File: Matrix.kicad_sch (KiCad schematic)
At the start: 72 parts, among them SW1 SW_Push, SW10 SW_Push, SW11 SW_Push, SW12 SW_Push, SW13 SW_Push, SW14 SW_Push, SW15 SW_Push, SW16 SW_Push, SW17 SW_Push, SW18 SW_Push, SW2 SW_Push, SW3 SW_Push, SW4 SW_Push, SW5 SW_Push, SW6 SW_Push, SW7 SW_Push, SW8 SW_Push, SW9 SW_Push

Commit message: update power mgmt
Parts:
- removed D10, D14, D15, D16, D17, D2, D22, D23, D24, D25, D3, D30, D31, D32, D33, D4, D8, D9: LED, LED_SMD:LED_0603_1608Metric_Pad1.05x0.95mm_HandSolder, symbol Device:LED
- removed R10, R11, R12, R13, R14, R15, R16, R17, R18, R19, R20, R21, R22, R23, R24, R25, R26, R27: 1 kohm, Resistor_SMD:R_0603_1608Metric_Pad0.98x0.95mm_HandSolder, symbol #inventree:RC0603FR-071KL
- added C10, C11, C12, C13, C14, C15, C16, C17, C18, C19, C20, C21, C23, C24, C25, C26, C7, C8, C9: 100N, Capacitor_SMD:C_0603_1608Metric_Pad1.08x0.95mm_HandSolder, symbol Device:C
- added D10, D14, D15, D16, D17, D22, D23, D24, D25, D3, D30, D31, D32, D44, D45, D46, D47, D8, D9: WS2812B, LED_SMD:LED_WS2812_PLCC6_5.0x5.0mm_P1.6mm, symbol LED:WS2812B
- added D2: CD4148W, Diode_SMD:D_0805_2012Metric_Pad1.15x1.40mm_HandSolder, symbol Diode:CD4148W
- added R10, R11, R12, R13: 500R, Resistor_SMD:R_0603_1608Metric_Pad0.98x0.95mm_HandSolder, symbol Device:R
- added SW20: SW_Push, personal:Gateron_Milky_Yellow, symbol Switch:SW_Push
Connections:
- net KB_COL_1 is gone; now on net KB_COL_0: SW4.1, SW5.1, SW6.1
- net KB_COL_2 is gone; now on net KB_COL_0: SW10.1, SW7.1, SW8.1, SW9.1
- net KB_COL_3 is gone; now on net KB_COL_0: SW11.1, SW12.1, SW13.1, SW14.1
- net KB_COL_4 is gone; now on net KB_COL_0: SW15.1, SW16.1, SW17.1, SW18.1
- net KB_ROW_0 is gone; now on net KB_COL_0: D11.1 (K), D18.1 (K), D26.1 (K), D34.1 (K), D5.1 (K)
- net GND: now also C10.1, C11.1, C12.1, C13.1, C14.1, C15.1, C16.1, C17.1, C18.1, C19.1, C20.1, C21.1, C23.1, C24.1, C25.1, C26.1, C7.1, C8.1, C9.1, D10.3 (VSS), D14.3 (VSS), D15.3 (VSS), D16.3 (VSS), D17.3 (VSS), D22.3 (VSS), D23.3 (VSS), D24.3 (VSS), D25.3 (VSS), D3.3 (VSS), D30.3 (VSS), D31.3 (VSS), D32.3 (VSS), D44.3 (VSS), D45.3 (VSS), D46.3 (VSS), D47.3 (VSS), D8.3 (VSS), D9.3 (VSS)
- net KB_COL_0: now also SW20.1
- net KB_ROW_3: now also D2.1 (K)
- new net: D3.4 (DIN), R10.2
- new net: D24.4 (DIN), R12.2
- new net: D25.2 (DOUT), D30.4 (DIN)
- new net: D24.2 (DOUT), D25.4 (DIN)
- new net: D10.4 (DIN), D9.2 (DOUT)
- new net: D8.2 (DOUT), D9.4 (DIN)
- new net: D45.2 (DOUT), D46.4 (DIN)
- new net: D44.2 (DOUT), D45.4 (DIN)
- new net: D30.2 (DOUT), D31.4 (DIN)
- new net: D10.2 (DOUT), D14.4 (DIN)
- new net: D15.4 (DIN), R11.2
- new net: D3.2 (DOUT), D8.4 (DIN)
- new net: D16.2 (DOUT), D17.4 (DIN)
- new net: D15.2 (DOUT), D16.4 (DIN)
- new net: D31.2 (DOUT), D32.4 (DIN)
- new net: D22.2 (DOUT), D23.4 (DIN)
- new net: D17.2 (DOUT), D22.4 (DIN)
- new net: D46.2 (DOUT), D47.4 (DIN)
- new net: D44.4 (DIN), R13.2
- new net: D2.2 (A), SW20.2
- new net +5V: C10.2, C11.2, C12.2, C13.2, C14.2, C15.2, C16.2, C17.2, C18.2, C19.2, C20.2, C21.2, C23.2, C24.2, C25.2, C26.2, C7.2, C8.2, C9.2, D10.1 (VDD), D14.1 (VDD), D15.1 (VDD), D16.1 (VDD), D17.1 (VDD), D22.1 (VDD), D23.1 (VDD), D24.1 (VDD), D25.1 (VDD), D3.1 (VDD), D30.1 (VDD), D31.1 (VDD), D32.1 (VDD), D44.1 (VDD), D45.1 (VDD), D46.1 (VDD), D47.1 (VDD), D8.1 (VDD), D9.1 (VDD)
- new net LEDDATA0: R10.1
- new net LEDDATA1: R11.1
- new net LEDDATA2: R12.1
- new net LEDDATA3: R13.1
- no-connect marks 0 -> 4
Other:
- moved on the sheet: D11, D12, D13, D18, D19, D20, D21, D26, D27, D28, D29, D34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

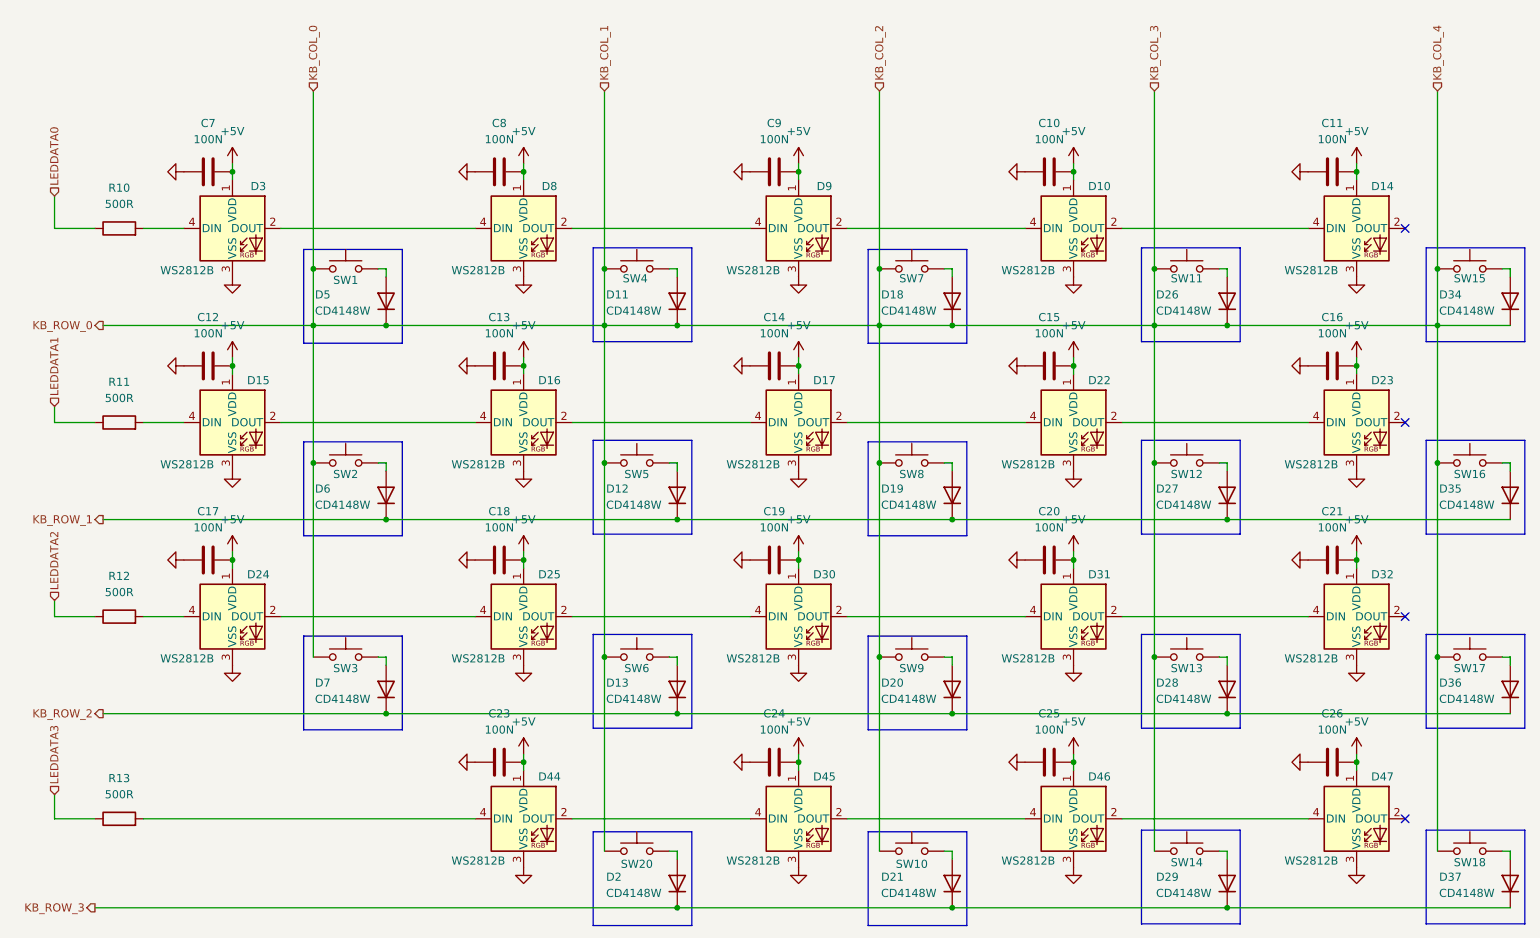
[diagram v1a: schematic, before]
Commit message: finish preliminary schematic
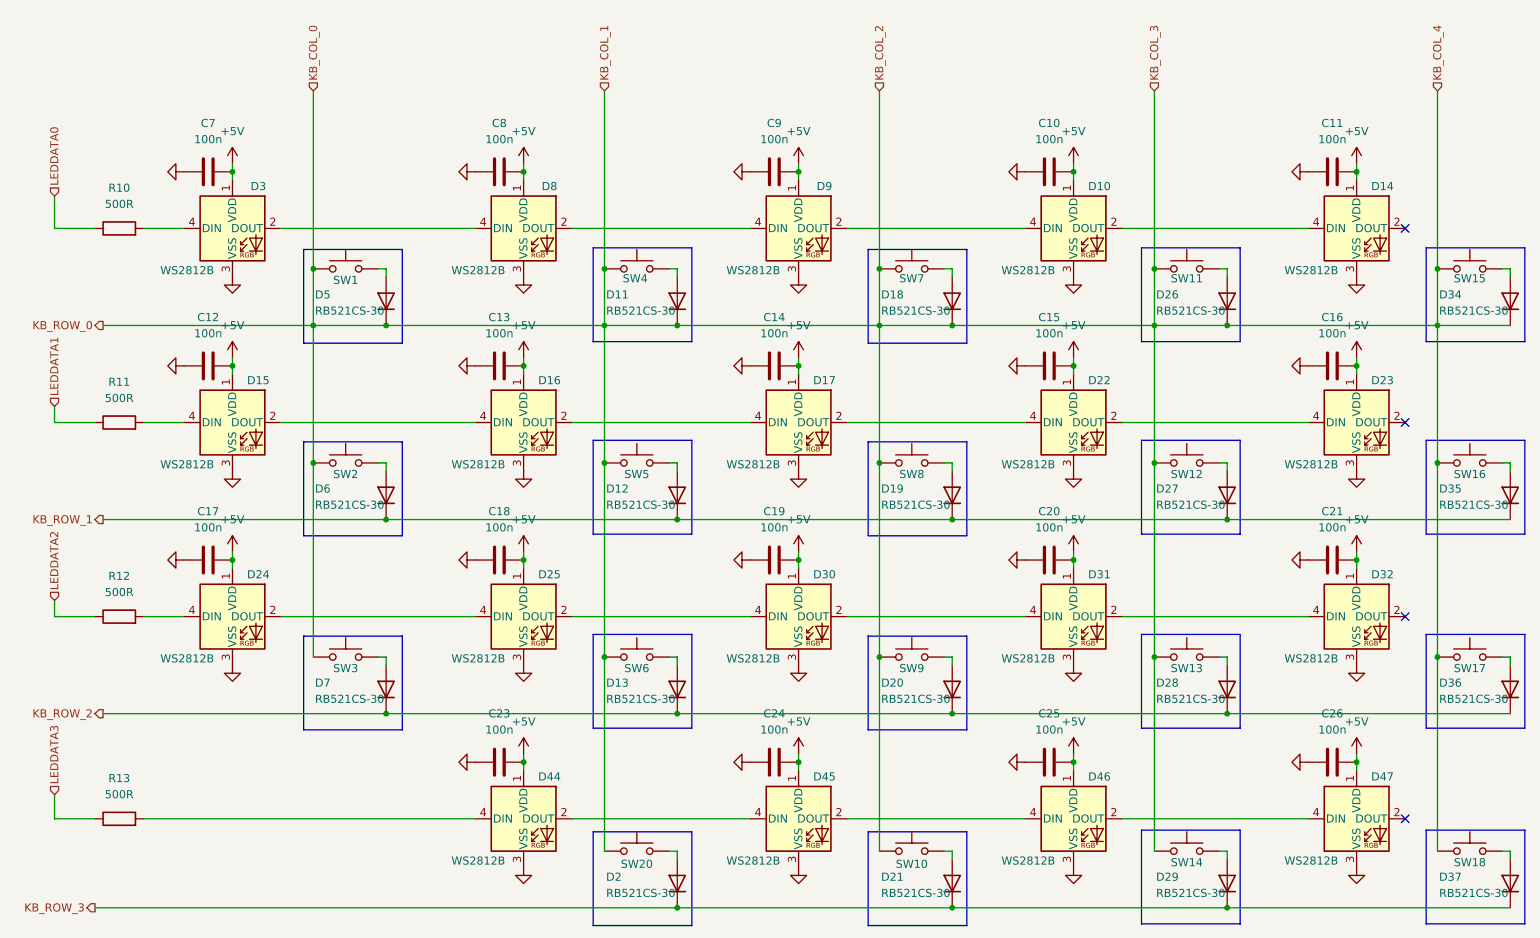
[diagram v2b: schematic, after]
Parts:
- C10, C11, C12, C13, C14, C15, C16, C17, C18, C19, C20, C21, C23, C24, C25, C26, C7, C8, C9: value 100N -> 100n
- D10, D14, D15, D16, D17, D22, D23, D24, D25, D3, D30, D31, D32, D44, D45, D46, D47, D8, D9: footprint LED_SMD:LED_WS2812_PLCC6_5.0x5.0mm_P1.6mm -> LED_SMD:LED_WS2812B_PLCC4_5.0x5.0mm_P3.2mm
- D11, D12, D13, D18, D19, D2, D20, D21, D26, D27, D28, D29, D34, D35, D36, D37, D5, D6, D7: value CD4148W -> RB521CS-30; footprint Diode_SMD:D_0805_2012Metric_Pad1.15x1.40mm_HandSolder -> Diode_SMD:D_SOD-923; InvenTree 64 -> (none)

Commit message: amend UVLO values
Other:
- company: (none) -> Daniel (steewBSD)
- title: (none) -> Tastatur the BLE Keyboard
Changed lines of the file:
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@@
 	(generator_version "9.0")
 	(paper "A4")
+	(title_block
+		(title "Tastatur the BLE Keyboard")
+		(date "2025-07-18")
+		(rev "0")
+		(company "Daniel (steewBSD)")
+	)
 	(rectangle
 		(start 235.712 113.284)

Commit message: finish initial placement
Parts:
- D251: renamed from D3; value WS2812B -> SK6805-EC15; footprint LED_SMD:LED_WS2812B_PLCC4_5.0x5.0mm_P3.2mm -> LED_SMD:LED_SK6812_EC15_1.5x1.5mm; symbol LED:WS2812B -> LED:SK6805; LCSC C22461793 -> C2890035; PN XL-5050RGBC-WS2812B-S -> SK6805-EC15
- D252: renamed from D8; value WS2812B -> SK6805-EC15; footprint LED_SMD:LED_WS2812B_PLCC4_5.0x5.0mm_P3.2mm -> LED_SMD:LED_SK6812_EC15_1.5x1.5mm; symbol LED:WS2812B -> LED:SK6805; LCSC C22461793 -> C2890035; PN XL-5050RGBC-WS2812B-S -> SK6805-EC15
- D253: renamed from D9; value WS2812B -> SK6805-EC15; footprint LED_SMD:LED_WS2812B_PLCC4_5.0x5.0mm_P3.2mm -> LED_SMD:LED_SK6812_EC15_1.5x1.5mm; symbol LED:WS2812B -> LED:SK6805; LCSC C22461793 -> C2890035; PN XL-5050RGBC-WS2812B-S -> SK6805-EC15
- D254: renamed from D10; value WS2812B -> SK6805-EC15; footprint LED_SMD:LED_WS2812B_PLCC4_5.0x5.0mm_P3.2mm -> LED_SMD:LED_SK6812_EC15_1.5x1.5mm; symbol LED:WS2812B -> LED:SK6805; LCSC C22461793 -> C2890035; PN XL-5050RGBC-WS2812B-S -> SK6805-EC15
- D255: renamed from D14; value WS2812B -> SK6805-EC15; footprint LED_SMD:LED_WS2812B_PLCC4_5.0x5.0mm_P3.2mm -> LED_SMD:LED_SK6812_EC15_1.5x1.5mm; symbol LED:WS2812B -> LED:SK6805; LCSC C22461793 -> C2890035; PN XL-5050RGBC-WS2812B-S -> SK6805-EC15
- D256: renamed from D15; value WS2812B -> SK6805-EC15; footprint LED_SMD:LED_WS2812B_PLCC4_5.0x5.0mm_P3.2mm -> LED_SMD:LED_SK6812_EC15_1.5x1.5mm; symbol LED:WS2812B -> LED:SK6805; LCSC C22461793 -> C2890035; PN XL-5050RGBC-WS2812B-S -> SK6805-EC15
- D257: renamed from D16; value WS2812B -> SK6805-EC15; footprint LED_SMD:LED_WS2812B_PLCC4_5.0x5.0mm_P3.2mm -> LED_SMD:LED_SK6812_EC15_1.5x1.5mm; symbol LED:WS2812B -> LED:SK6805; LCSC C22461793 -> C2890035; PN XL-5050RGBC-WS2812B-S -> SK6805-EC15
- D258: renamed from D17; value WS2812B -> SK6805-EC15; footprint LED_SMD:LED_WS2812B_PLCC4_5.0x5.0mm_P3.2mm -> LED_SMD:LED_SK6812_EC15_1.5x1.5mm; symbol LED:WS2812B -> LED:SK6805; LCSC C22461793 -> C2890035; PN XL-5050RGBC-WS2812B-S -> SK6805-EC15
- D259: renamed from D22; value WS2812B -> SK6805-EC15; footprint LED_SMD:LED_WS2812B_PLCC4_5.0x5.0mm_P3.2mm -> LED_SMD:LED_SK6812_EC15_1.5x1.5mm; symbol LED:WS2812B -> LED:SK6805; LCSC C22461793 -> C2890035; PN XL-5050RGBC-WS2812B-S -> SK6805-EC15
- D260: renamed from D23; value WS2812B -> SK6805-EC15; footprint LED_SMD:LED_WS2812B_PLCC4_5.0x5.0mm_P3.2mm -> LED_SMD:LED_SK6812_EC15_1.5x1.5mm; symbol LED:WS2812B -> LED:SK6805; LCSC C22461793 -> C2890035; PN XL-5050RGBC-WS2812B-S -> SK6805-EC15
- D261: renamed from D24; value WS2812B -> SK6805-EC15; footprint LED_SMD:LED_WS2812B_PLCC4_5.0x5.0mm_P3.2mm -> LED_SMD:LED_SK6812_EC15_1.5x1.5mm; symbol LED:WS2812B -> LED:SK6805; LCSC C22461793 -> C2890035; PN XL-5050RGBC-WS2812B-S -> SK6805-EC15
- D262: renamed from D25; value WS2812B -> SK6805-EC15; footprint LED_SMD:LED_WS2812B_PLCC4_5.0x5.0mm_P3.2mm -> LED_SMD:LED_SK6812_EC15_1.5x1.5mm; symbol LED:WS2812B -> LED:SK6805; LCSC C22461793 -> C2890035; PN XL-5050RGBC-WS2812B-S -> SK6805-EC15
- D263: renamed from D30; value WS2812B -> SK6805-EC15; footprint LED_SMD:LED_WS2812B_PLCC4_5.0x5.0mm_P3.2mm -> LED_SMD:LED_SK6812_EC15_1.5x1.5mm; symbol LED:WS2812B -> LED:SK6805; LCSC C22461793 -> C2890035; PN XL-5050RGBC-WS2812B-S -> SK6805-EC15
- D264: renamed from D31; value WS2812B -> SK6805-EC15; footprint LED_SMD:LED_WS2812B_PLCC4_5.0x5.0mm_P3.2mm -> LED_SMD:LED_SK6812_EC15_1.5x1.5mm; symbol LED:WS2812B -> LED:SK6805; LCSC C22461793 -> C2890035; PN XL-5050RGBC-WS2812B-S -> SK6805-EC15
- D265: renamed from D32; value WS2812B -> SK6805-EC15; footprint LED_SMD:LED_WS2812B_PLCC4_5.0x5.0mm_P3.2mm -> LED_SMD:LED_SK6812_EC15_1.5x1.5mm; symbol LED:WS2812B -> LED:SK6805; LCSC C22461793 -> C2890035; PN XL-5050RGBC-WS2812B-S -> SK6805-EC15
- D266: renamed from D44; value WS2812B -> SK6805-EC15; footprint LED_SMD:LED_WS2812B_PLCC4_5.0x5.0mm_P3.2mm -> LED_SMD:LED_SK6812_EC15_1.5x1.5mm; symbol LED:WS2812B -> LED:SK6805; LCSC C22461793 -> C2890035; PN XL-5050RGBC-WS2812B-S -> SK6805-EC15
- D267: renamed from D45; value WS2812B -> SK6805-EC15; footprint LED_SMD:LED_WS2812B_PLCC4_5.0x5.0mm_P3.2mm -> LED_SMD:LED_SK6812_EC15_1.5x1.5mm; symbol LED:WS2812B -> LED:SK6805; LCSC C22461793 -> C2890035; PN XL-5050RGBC-WS2812B-S -> SK6805-EC15
- D268: renamed from D46; value WS2812B -> SK6805-EC15; footprint LED_SMD:LED_WS2812B_PLCC4_5.0x5.0mm_P3.2mm -> LED_SMD:LED_SK6812_EC15_1.5x1.5mm; symbol LED:WS2812B -> LED:SK6805; LCSC C22461793 -> C2890035; PN XL-5050RGBC-WS2812B-S -> SK6805-EC15
- D269: renamed from D47; value WS2812B -> SK6805-EC15; footprint LED_SMD:LED_WS2812B_PLCC4_5.0x5.0mm_P3.2mm -> LED_SMD:LED_SK6812_EC15_1.5x1.5mm; symbol LED:WS2812B -> LED:SK6805; LCSC C22461793 -> C2890035; PN XL-5050RGBC-WS2812B-S -> SK6805-EC15
- SW201: renamed from SW1; footprint personal:Gateron_Milky_Yellow -> PCM_Switch_Keyboard_Cherry_MX:SW_Cherry_MX_PCB_1.00u
- SW202: renamed from SW4; footprint personal:Gateron_Milky_Yellow -> PCM_Switch_Keyboard_Cherry_MX:SW_Cherry_MX_PCB_1.00u
- SW203: renamed from SW7; footprint personal:Gateron_Milky_Yellow -> PCM_Switch_Keyboard_Cherry_MX:SW_Cherry_MX_PCB_1.00u
- SW204: renamed from SW11; footprint personal:Gateron_Milky_Yellow -> PCM_Switch_Keyboard_Cherry_MX:SW_Cherry_MX_PCB_1.00u
- SW205: renamed from SW15; footprint personal:Gateron_Milky_Yellow -> PCM_Switch_Keyboard_Cherry_MX:SW_Cherry_MX_PCB_1.00u
- SW206: renamed from SW2; footprint personal:Gateron_Milky_Yellow -> PCM_Switch_Keyboard_Cherry_MX:SW_Cherry_MX_PCB_1.00u
- SW207: renamed from SW5; footprint personal:Gateron_Milky_Yellow -> PCM_Switch_Keyboard_Cherry_MX:SW_Cherry_MX_PCB_1.00u
- SW208: renamed from SW8; footprint personal:Gateron_Milky_Yellow -> PCM_Switch_Keyboard_Cherry_MX:SW_Cherry_MX_PCB_1.00u
- SW209: renamed from SW12; footprint personal:Gateron_Milky_Yellow -> PCM_Switch_Keyboard_Cherry_MX:SW_Cherry_MX_PCB_1.00u
- SW210: renamed from SW16; footprint personal:Gateron_Milky_Yellow -> PCM_Switch_Keyboard_Cherry_MX:SW_Cherry_MX_PCB_1.00u
- SW211: renamed from SW3; footprint personal:Gateron_Milky_Yellow -> PCM_Switch_Keyboard_Cherry_MX:SW_Cherry_MX_PCB_1.00u
- SW212: renamed from SW6; footprint personal:Gateron_Milky_Yellow -> PCM_Switch_Keyboard_Cherry_MX:SW_Cherry_MX_PCB_1.00u
- SW213: renamed from SW9; footprint personal:Gateron_Milky_Yellow -> PCM_Switch_Keyboard_Cherry_MX:SW_Cherry_MX_PCB_1.00u
- SW214: renamed from SW13; footprint personal:Gateron_Milky_Yellow -> PCM_Switch_Keyboard_Cherry_MX:SW_Cherry_MX_PCB_1.00u
- SW215: renamed from SW17; footprint personal:Gateron_Milky_Yellow -> PCM_Switch_Keyboard_Cherry_MX:SW_Cherry_MX_PCB_1.00u
- SW216: renamed from SW20; footprint personal:Gateron_Milky_Yellow -> PCM_Switch_Keyboard_Cherry_MX:SW_Cherry_MX_PCB_1.00u
- SW217: renamed from SW10; footprint personal:Gateron_Milky_Yellow -> PCM_Switch_Keyboard_Cherry_MX:SW_Cherry_MX_PCB_1.00u
- SW218: renamed from SW14; footprint personal:Gateron_Milky_Yellow -> PCM_Switch_Keyboard_Cherry_MX:SW_Cherry_MX_PCB_1.00u
- SW219: renamed from SW18; footprint personal:Gateron_Milky_Yellow -> PCM_Switch_Keyboard_Cherry_MX:SW_Cherry_MX_PCB_1.00u
- renumbered C7 to C201, C8 to C202, C9 to C203, C10 to C204, C11 to C205, C12 to C206, C13 to C207, C14 to C208, C15 to C209, C16 to C210, C17 to C211, C18 to C212, C19 to C213, C20 to C214, C21 to C215, C23 to C216, C24 to C217, C25 to C218, C26 to C219, D5 to D201, D11 to D202, D18 to D203, D26 to D204, D34 to D205, D6 to D206, D12 to D207, D19 to D208, D27 to D209, D35 to D210, D7 to D211, D13 to D212, D20 to D213, D28 to D214, D36 to D215, D2 to D216, D21 to D217, D29 to D218, D37 to D219, R10 to R201, R11 to R202, R12 to R203, R13 to R204
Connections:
- net +5V: now also D251.4 (VDD), D252.4 (VDD), D253.4 (VDD), D254.4 (VDD), D255.4 (VDD), D256.4 (VDD), D257.4 (VDD), D258.4 (VDD), D259.4 (VDD), D260.4 (VDD), D261.4 (VDD), D262.4 (VDD), D263.4 (VDD), D264.4 (VDD), D265.4 (VDD), D266.4 (VDD), D267.4 (VDD), D268.4 (VDD), D269.4 (VDD); no longer D251.1 (VDD), D252.1 (VDD), D253.1 (VDD), D254.1 (VDD), D255.1 (VDD), D256.1 (VDD), D257.1 (VDD), D258.1 (VDD), D259.1 (VDD), D260.1 (VDD), D261.1 (VDD), D262.1 (VDD), D263.1 (VDD), D264.1 (VDD), D265.1 (VDD), D266.1 (VDD), D267.1 (VDD), D268.1 (VDD), D269.1 (VDD)
- net GND: now also D251.2 (VSS), D252.2 (VSS), D253.2 (VSS), D254.2 (VSS), D255.2 (VSS), D256.2 (VSS), D257.2 (VSS), D258.2 (VSS), D259.2 (VSS), D260.2 (VSS), D261.2 (VSS), D262.2 (VSS), D263.2 (VSS), D264.2 (VSS), D265.2 (VSS), D266.2 (VSS), D267.2 (VSS), D268.2 (VSS), D269.2 (VSS); no longer D251.3 (VSS), D252.3 (VSS), D253.3 (VSS), D254.3 (VSS), D255.3 (VSS), D256.3 (VSS), D257.3 (VSS), D258.3 (VSS), D259.3 (VSS), D260.3 (VSS), D261.3 (VSS), D262.3 (VSS), D263.3 (VSS), D264.3 (VSS), D265.3 (VSS), D266.3 (VSS), D267.3 (VSS), D268.3 (VSS), D269.3 (VSS)
- net KB_COL_0: no longer D201.1 (K), D202.1 (K), D203.1 (K), D204.1 (K), D205.1 (K), SW202.1, SW203.1, SW204.1, SW205.1, SW207.1, SW208.1, SW209.1, SW210.1, SW212.1, SW213.1, SW214.1, SW215.1, SW216.1, SW217.1, SW218.1, SW219.1
- net at R201.2: now also D251.3 (DIN); no longer D251.4 (DIN)
- net at R203.2: now also D261.3 (DIN); no longer D261.4 (DIN)
- net at R202.2: now also D256.3 (DIN); no longer D256.4 (DIN)
- net at R204.2: now also D266.3 (DIN); no longer D266.4 (DIN)
- new net: D262.1 (DOUT), D263.3 (DIN)
- new net: D261.1 (DOUT), D262.3 (DIN)
- new net: D253.1 (DOUT), D254.3 (DIN)
- new net: D252.1 (DOUT), D253.3 (DIN)
- new net: D267.1 (DOUT), D268.3 (DIN)
- new net: D266.1 (DOUT), D267.3 (DIN)
- new net: D263.1 (DOUT), D264.3 (DIN)
- new net: D254.1 (DOUT), D255.3 (DIN)
- new net: D251.1 (DOUT), D252.3 (DIN)
- new net: D257.1 (DOUT), D258.3 (DIN)
- new net: D256.1 (DOUT), D257.3 (DIN)
- new net: D264.1 (DOUT), D265.3 (DIN)
- new net: D259.1 (DOUT), D260.3 (DIN)
- new net: D258.1 (DOUT), D259.3 (DIN)
- new net: D268.1 (DOUT), D269.3 (DIN)
- new net KB_COL_1: SW202.1, SW207.1, SW212.1, SW216.1
- new net KB_COL_2: SW203.1, SW208.1, SW213.1, SW217.1
- new net KB_COL_3: SW204.1, SW209.1, SW214.1, SW218.1
- new net KB_COL_4: SW205.1, SW210.1, SW215.1, SW219.1
- new net KB_ROW_0: D201.1 (K), D202.1 (K), D203.1 (K), D204.1 (K), D205.1 (K)
